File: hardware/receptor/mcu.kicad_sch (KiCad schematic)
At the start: 15 parts, among them J1 I2C, SW1 RESET, SW2 BOOT, U1 ESP32-C3-MINI-1-H4X

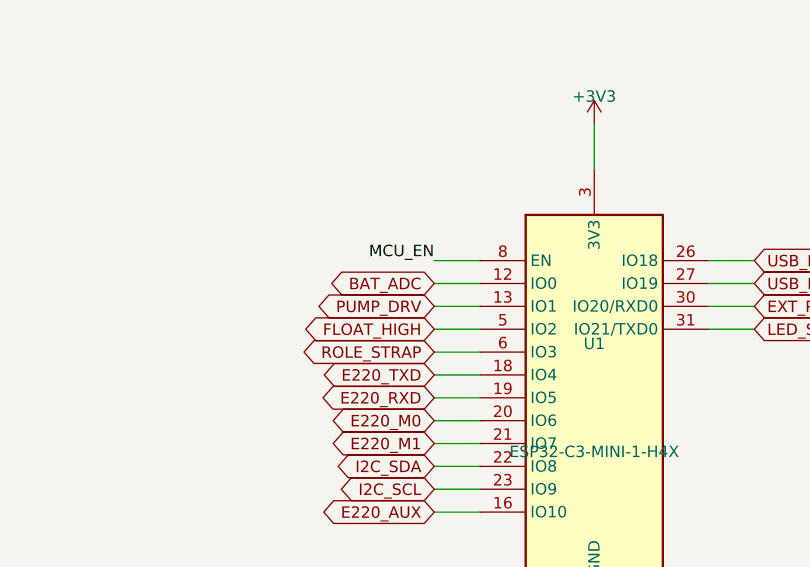
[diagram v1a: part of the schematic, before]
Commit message: feat(hw): jack 12 V com buck AP63205, roteador proprio e serigrafia padronizada (receptor roteado; emissor com 1 net aberta)
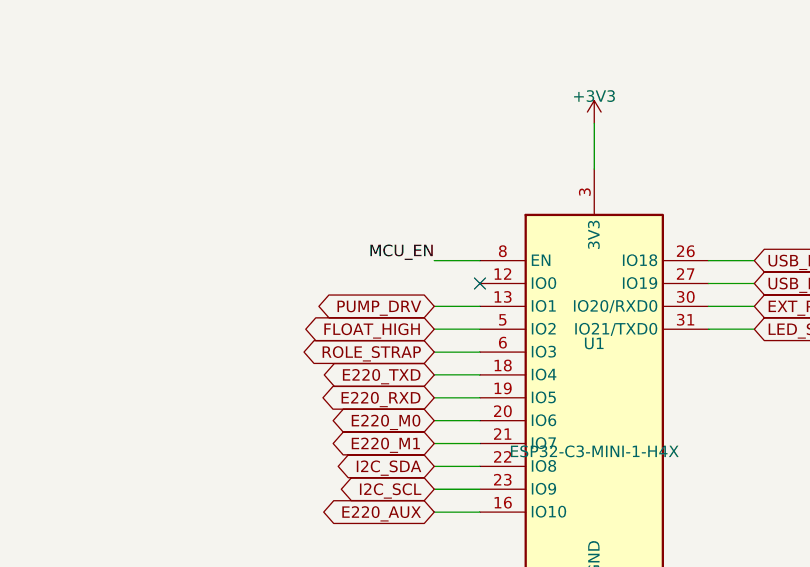
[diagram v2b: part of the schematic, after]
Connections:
- net BAT_ADC: no longer names the net of U1.12 (IO0)
- no-connect marks 0 -> 1
